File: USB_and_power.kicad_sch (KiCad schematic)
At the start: 44 parts, among them J1 USB_B_Micro, U1 LM2594M-3.3, U2 93LC54B, U3 FT4232H, Y1 12MHz

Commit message: After update to kicak 9.0
Signed-off-by: Marc Kelly <mpkelly@achenar.co.uk>
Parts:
- C1: MFN (none) -> Kemet; MFP (none) -> C0603C103J3RACAUTO; SUPPLIER (none) -> Mouser; SUPPLIER_LINK (none) -> https://www.mouser.co.uk/ProductDetail/KEMET/C0603C103J3RAC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; SUPPLIER_PN (none) -> 80-C0603C103J3RAUTO
- C10, C11, C12, C13, C14, C15, C16, C17, C18, C5, C7, C9: MFN (none) -> Kemet; MFP (none) -> C0603C104J4RACTU; SUPPLIER (none) -> Mouser; SUPPLIER_LINK (none) -> https://www.mouser.co.uk/ProductDetail/KEMET/C0603C104J4RAC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; SUPPLIER_PN (none) -> 80-C0603C104J4R
- C2: MFN (none) -> Kyocera AVX; MFP (none) -> TAJB686K010RNJ; Notes (none) -> 10V rated; SUPPLIER (none) -> Mouser; SUPPLIER_LINK (none) -> https://www.mouser.co.uk/ProductDetail/Kyocera-AVX/TAJB686K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; SUPPLIER_PN (none) -> 581-TAJB686K010RNJ
- C3: MFN (none) -> Panasonic; MFP (none) -> EEE-FN1A151L; Notes (none) -> 10V, 150uF; SUPPLIER (none) -> Mouser; SUPPLIER_LINK (none) -> https://www.mouser.co.uk/ProductDetail/Panasonic/EEE-FN1A15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; SUPPLIER_PN (none) -> 667-EEE-FN1A151L
- C4, C6: MFN (none) -> Kyocera AVX; MFP (none) -> F981C475MMA; SUPPLIER (none) -> Mouser; SUPPLIER_LINK (none) -> https://www.mouser.co.uk/ProductDetail/Kyocera-AVX/F981C475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; SUPPLIER_PN (none) -> 647-F981C475MMA
- C8: MFN (none) -> Kyocera AVX; MFP (none) -> TLCL335M016RTA; SUPPLIER (none) -> Mouser; SUPPLIER_LINK (none) -> https://www.mouser.co.uk/ProductDetail/Kyocera-AVX/TLCL335M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; SUPPLIER_PN (none) -> 581-TLCL335M016RTA
- D1: MFN (none) -> Samtech; MFP (none) -> RCLAMP0582BQTCT; SUPPLIER (none) -> Mouser; SUPPLIER_LINK (none) -> https://www.mouser.co.uk/ProductDetail/Semtech/RCLAMP0582BQ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; SUPPLIER_PN (none) -> 947-RCLAMP0582BQTCT
- D12, D2: MFN (none) -> Wurth; MFP (none) -> 155060GS75300; SUPPLIER (none) -> Mouser; SUPPLIER_LINK (none) -> https://www.mouser.co.uk/ProductDetail/Wurth-Elektronik/155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; SUPPLIER_PN (none) -> 710-155060GS75300
- D13: MFN (none) -> Wurth; MFP (none) -> 150060GS55040; SUPPLIER (none) -> Mouser; SUPPLIER_LINK (none) -> https://www.mouser.co.uk/ProductDetail/Wurth-Elektronik/150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; SUPPLIER_PN (none) -> 710-150060GS55040
- D3: MFN (none) -> MCC; MFP (none) -> MBRX120LF-TP; SUPPLIER (none) -> Mouser; SUPPLIER_LINK (none) -> https://www.mouser.co.uk/ProductDetail/Micro-Commercial-Com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; SUPPLIER_PN (none) -> 833-MBRX120LF-TP
- F1: MFN (none) -> Bel Fuse; MFP (none) -> 0ZCJ0075AF2E; SUPPLIER (none) -> Mouser; SUPPLIER_LINK (none) -> https://www.mouser.co.uk/ProductDetail/Bel-Fuse/0ZCJ0075AF2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; SUPPLIER_PN (none) -> 530-0ZCJ0075AF2E
- J1: MFN (none) -> Ampheonol; MFP (none) -> 10103594-0001LF; SUPPLIER (none) -> Mouser; SUPPLIER_LINK (none) -> https://www.mouser.co.uk/ProductDetail/Amphenol-FCI/1010359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; SUPPLIER_PN (none) -> 649-10103594-0001LF
- L1, L3, L4: MFN (none) -> TDK; MFP (none) -> MLZ1608DR47DTD25; Notes (none) -> 470-680nH Rage. 500-1000mA; SUPPLIER (none) -> Mouser; SUPPLIER_LINK (none) -> https://www.mouser.co.uk/ProductDetail/TDK/MLZ1608DR47DTD25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; SUPPLIER_PN (none) -> 810-MLZ1608DR47DTD25
- L2: MFN (none) -> Bourns; MFP (none) -> SRN6045-101M; SUPPLIER (none) -> Mouser; SUPPLIER_LINK (none) -> https://www.mouser.co.uk/ProductDetail/Bourns/SRN6045-101M?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; SUPPLIER_PN (none) -> 652-SRN6045-101M
- R1, R8: MFN (none) -> Generic; SUPPLIER (none) -> Mouser; SUPPLIER_LINK (none) -> https://www.mouser.co.uk/ProductDetail/Susumu/YJP-1608-R001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; SUPPLIER_PN (none) -> 754-YJP-1608-R001
- R2: MFN (none) -> Generic; SUPPLIER (none) -> Mouser; SUPPLIER_LINK (none) -> https://www.mouser.co.uk/ProductDetail/YAGEO/RT0603FRE0710R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; SUPPLIER_PN (none) -> 603-RT0603FRE0710RL
- R20, R29, R30: MFN (none) -> Generic; SUPPLIER (none) -> Mouser; SUPPLIER_PN (none) -> 754-RG1608P-331-BT5
- R3: value R10 -> 10R; MFN (none) -> Generic; SUPPLIER (none) -> Mouser; SUPPLIER_LINK (none) -> https://www.mouser.co.uk/ProductDetail/YAGEO/RT0603FRE0710R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; SUPPLIER_PN (none) -> 603-RT0603FRE0710RL
- R4, R5: MFN (none) -> Generic; SUPPLIER (none) -> Mouser; SUPPLIER_LINK (none) -> https://www.mouser.co.uk/ProductDetail/YAGEO/RT0402FRE1310K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; SUPPLIER_PN (none) -> 603-RT0402FRE1310KL
- R6: MFN (none) -> Generic; SUPPLIER (none) -> Mouser; SUPPLIER_LINK (none) -> https://www.mouser.co.uk/ProductDetail/TE-Connectivity-Hols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; SUPPLIER_PN (none) -> 279-CPF0603F2K0C1
- R7: MFN (none) -> Generic; SUPPLIER (none) -> Mouser; SUPPLIER_PN (none) -> 603-RT0603DRE0712KL
- U1: MFN (none) -> TI; MFP (none) -> LM2594M-3.3/NOPB; SUPPLIER (none) -> Mouser; SUPPLIER_LINK (none) -> https://www.mouser.co.uk/ProductDetail/Texas-Instruments/LM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; SUPPLIER_PN (none) -> 926-LM2594MX33NOPB
- U3: MFN (none) -> FTDIChip; MFP (none) -> FT4232HL; SUPPLIER (none) -> Mouser; SUPPLIER_LINK (none) -> https://www.mouser.co.uk/c/semiconductors/interface-ics/usb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; SUPPLIER_PN (none) -> 895-FT4232HL-TRAY
- Y1: MFN (none) -> Vishy; MFP (none) -> XT9MNLANA12M; SUPPLIER (none) -> Mouser; SUPPLIER_LINK (none) -> https://www.mouser.co.uk/ProductDetail/Vishay-Dale/XT9MNLAN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; SUPPLIER_PN (none) -> 73-XT49M1200-S
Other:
- note added: "Inductors L1,2,3 should be ~470-680nH. 500-1000mA"

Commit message: Updated to remove the level shifters
Just have 3v3 ttl outputs for now, trancievers will be on different
boards
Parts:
- removed J1: USB_B_Micro, Connector_USB:USB_Micro-B_Amphenol_10103594-0001LF_Horizontal, symbol Connector:USB_B_Micro
- added J5: USB_C_Receptacle_USB2.0_14P, symbol Connector:USB_C_Receptacle_USB2.0_14P
- added R21, R22: 5k1, Resistor_SMD:R_0603_1608Metric_Pad0.98x0.95mm_HandSolder, symbol Device:R_Small
- renumbered C12 to C1, C4 to C10, C5 to C11, C6 to C12, C7 to C13, C1 to C14, C10 to C15, C8 to C16, C9 to C17, C11 to C18, C13 to C2, C14 to C3, C15 to C4, C16 to C5, C17 to C6, C18 to C7, C2 to C8, C3 to C9, D3 to D13, D2 to D14, D1 to D15, D12 to D16, D13 to D17, L3 to L1, L4 to L2, L2 to L3, L1 to L4, R20 to R15, R2 to R16, R3 to R17, R4 to R18, R7 to R19, R1 to R20, R5 to R23, R6 to R24, R29 to R25, R30 to R26, R8 to R27, U1 to U3, U3 to U4, U2 to U5
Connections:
- net D+: now also D15.1 (K), R17.2, J5.A6 (D+), J5.B6 (D+); no longer D15.2 (K), R16.2
- net D-: now also D15.2 (K), R16.2, J5.A7 (D-), J5.B7 (D-); no longer D15.1 (K), R17.2
- net GND: now also J5.A1 (GND), J5.A12 (GND), J5.B1 (GND), J5.B12 (GND), R21.2, R22.2
- net at F1.2: now also J5.A4 (VBUS), J5.A9 (VBUS), J5.B4 (VBUS), J5.B9 (VBUS)
- net at R20.1: now also J5.S1 (SHIELD)
- new net: J5.A5 (CC1), R22.1
- new net: J5.B5 (CC2), R21.1
- no-connect marks 4 -> 3
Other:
- moved on the sheet: C10, C11, C12, C13, C14, C8, C9, D13, D14, D15, F1, L1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

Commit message: Updated power leds and external protection on Serial
Signed-off-by: Marc Kelly <mpkelly@achenar.co.uk>
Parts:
- removed D14: G_LED, LED_SMD:LED_0603_1608Metric_Pad1.05x0.95mm_HandSolder, symbol Device:LED
- removed R15: 330R, Resistor_SMD:R_0603_1608Metric_Pad0.98x0.95mm_HandSolder, symbol Device:R_Small
- added C17: 100nF, Capacitor_SMD:C_0603_1608Metric_Pad1.08x0.95mm_HandSolder, symbol Device:C_Small
- added SW1: ResetButton, Button_Switch_SMD:SW_SPST_TS-1088-xR020, symbol Switch:SW_Push
- C8: footprint Capacitor_Tantalum_SMD:CP_EIA-3528-21_Kemet-B_Pad1.50x2.35mm_HandSolder -> Capacitor_Tantalum_SMD:CP_EIA-3528-21_Kemet-B_HandSolder
- J5: footprint (none) -> Connector_USB:USB_C_Receptacle_HRO_TYPE-C-31-M-12; symbol Connector:USB_C_Receptacle_USB2.0_14P -> Connector:USB_C_Receptacle_USB2.0_16P
- Y1: value 12MHz -> ABLS7M2-12.000MHZ-D2Y-T; footprint Crystal:Crystal_SMD_HC49-SD_HandSoldering -> Crystal:Crystal_SMD_ECS_CSM3X-2Pin_7.6x4.1mm
- renumbered C17 to C18, C18 to C19, D13 to D19, D15 to D20, D16 to D21, D17 to D22, R16 to R17, R17 to R18, R18 to R19, R19 to R20, R20 to R21, R21 to R22, R22 to R23, R23 to R24, R24 to R25, R25 to R26, R26 to R27, R27 to R28
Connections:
- net D_N: now also R17.1; no longer R18.1
- net D_P: now also R18.1; no longer R17.1
- net GND: now also C17.2, SW1.1
- net RESET#: now also C17.1, SW1.2
- no-connect marks 3 -> 5
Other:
- note added: "Decoupling Caps"
- moved on the sheet: R19

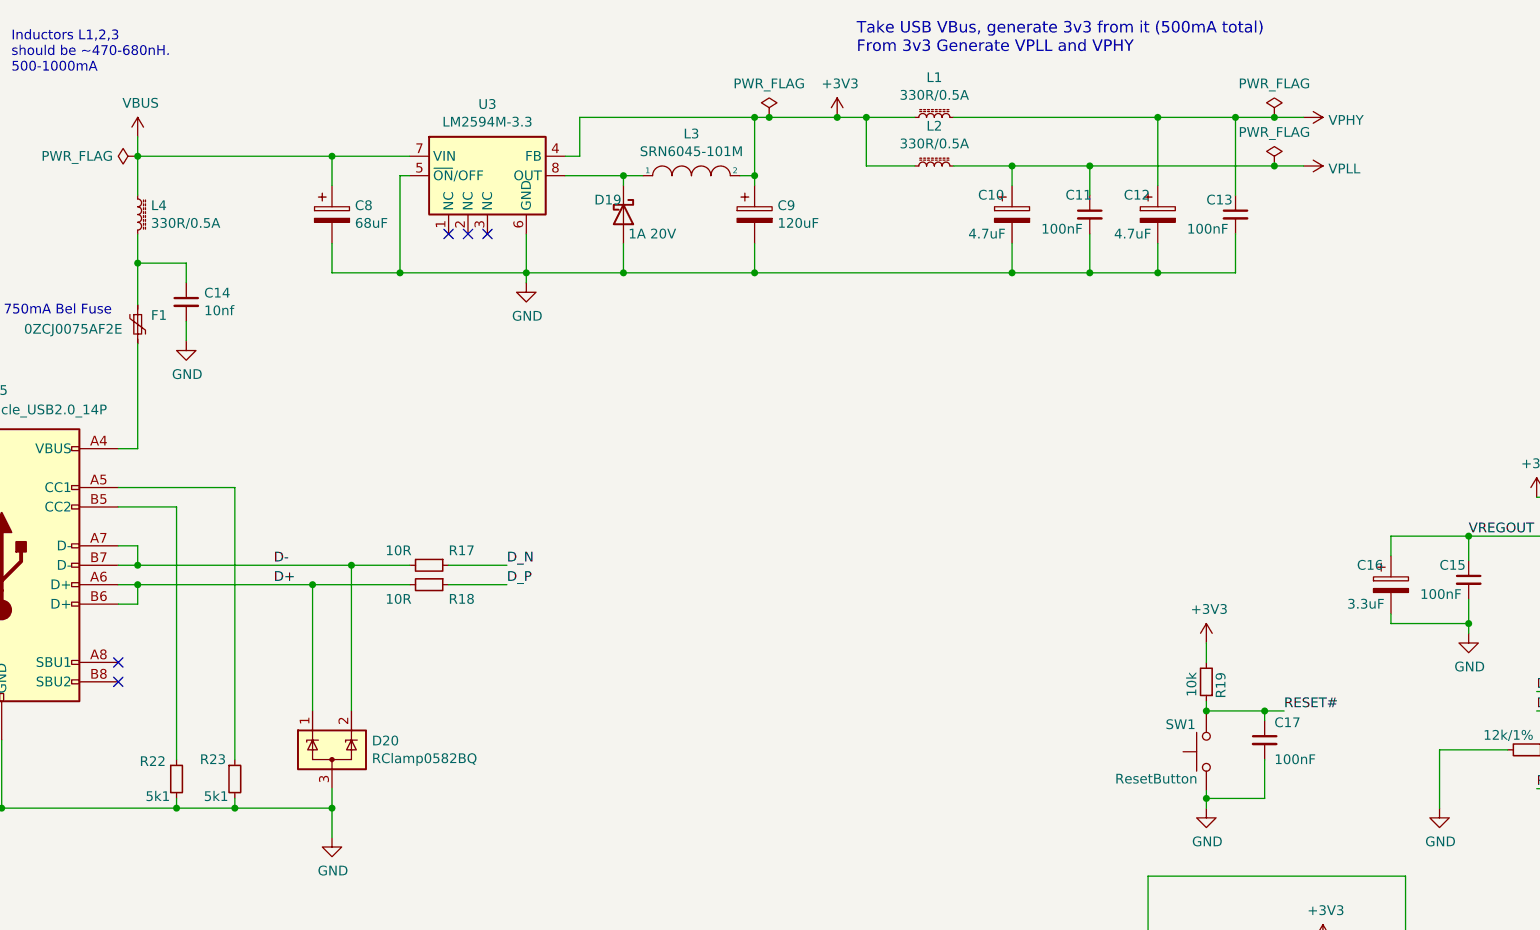
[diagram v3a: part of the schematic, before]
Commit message: Updated with the new design.
Removed all level translators.
4 sockets, 2x6 pin outputs
New PCB shape and routing
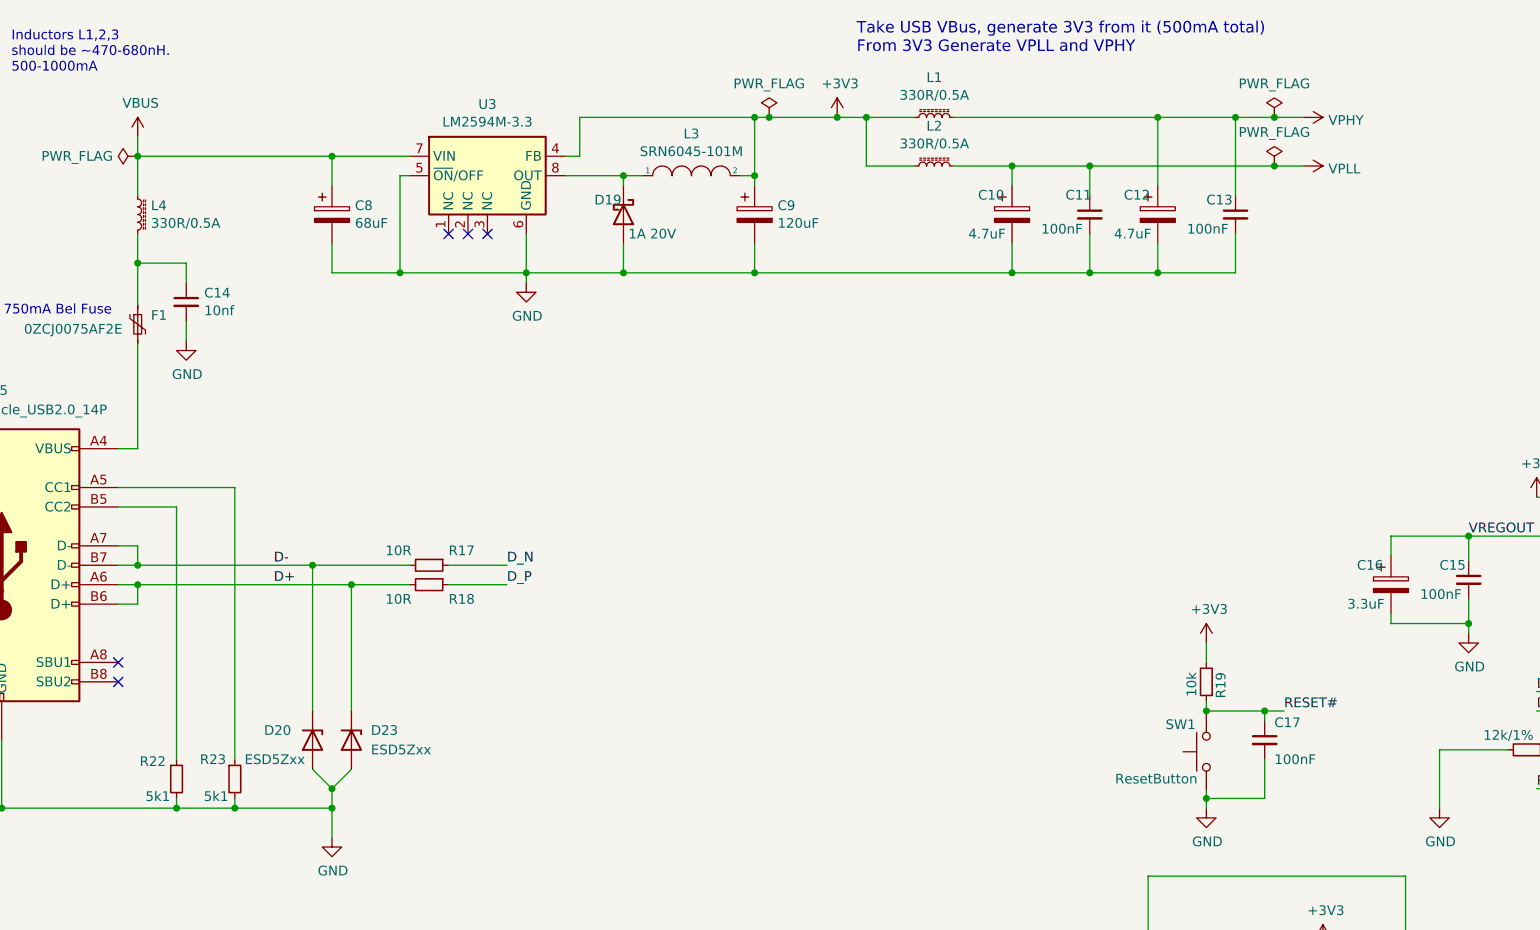
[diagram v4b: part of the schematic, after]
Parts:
- removed D20: RClamp0582BQ, Package_TO_SOT_SMD:SOT-416, symbol Power_Protection:SP0502BAJT
- added D20, D23: ESD5Zxx, Diode_SMD:D_SOD-523, symbol Diode:ESD5Zxx
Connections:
- net D+: now also D23.1 (K)
- net D-: now also D20.1 (K)
- net GND: now also D20.2 (A), D23.2 (A)
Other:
- note added: "Take USB VBus, generate 3V3 from it (500mA total) From 3V3 Generate VPLL and VPHY"
- note removed: "Take USB VBus, generate 3v3 from it (500mA total) From 3v3 Generate VPLL and VPHY"

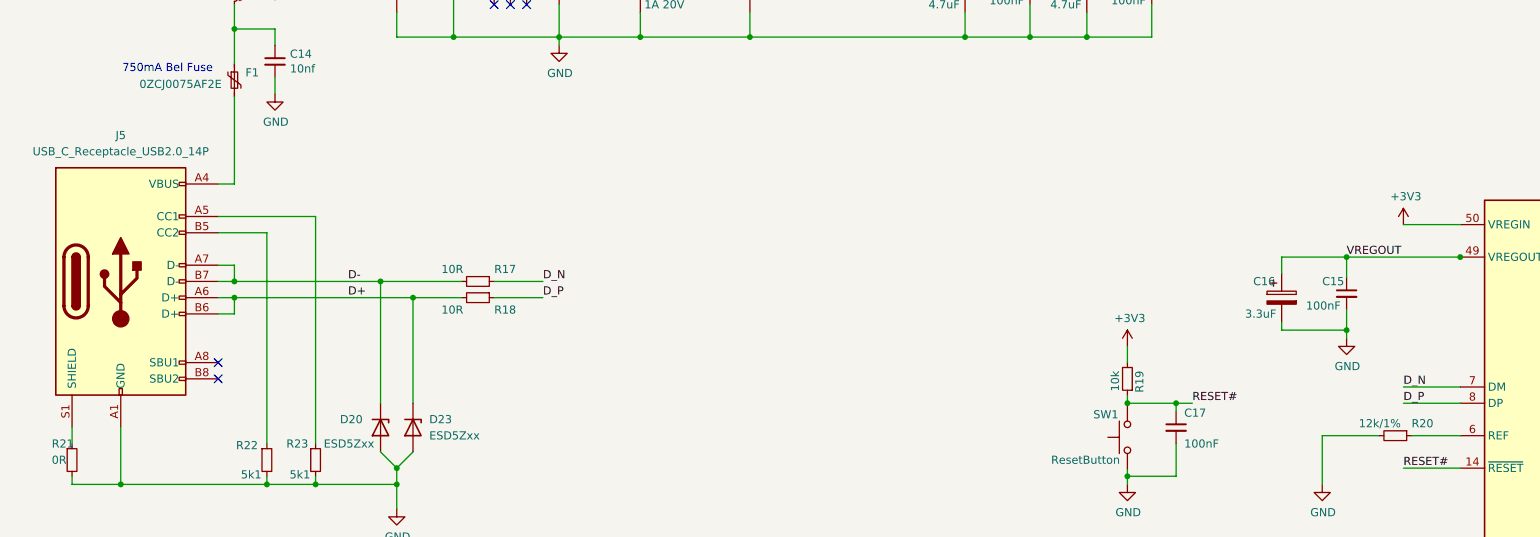
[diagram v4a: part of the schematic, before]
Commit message: Update schematics after moving to KiCad 10
Added some footprints to a local lib, as the silkscreen caused issues.

Signed-off-by: Marc Kelly <mpkelly@achenar.co.uk>
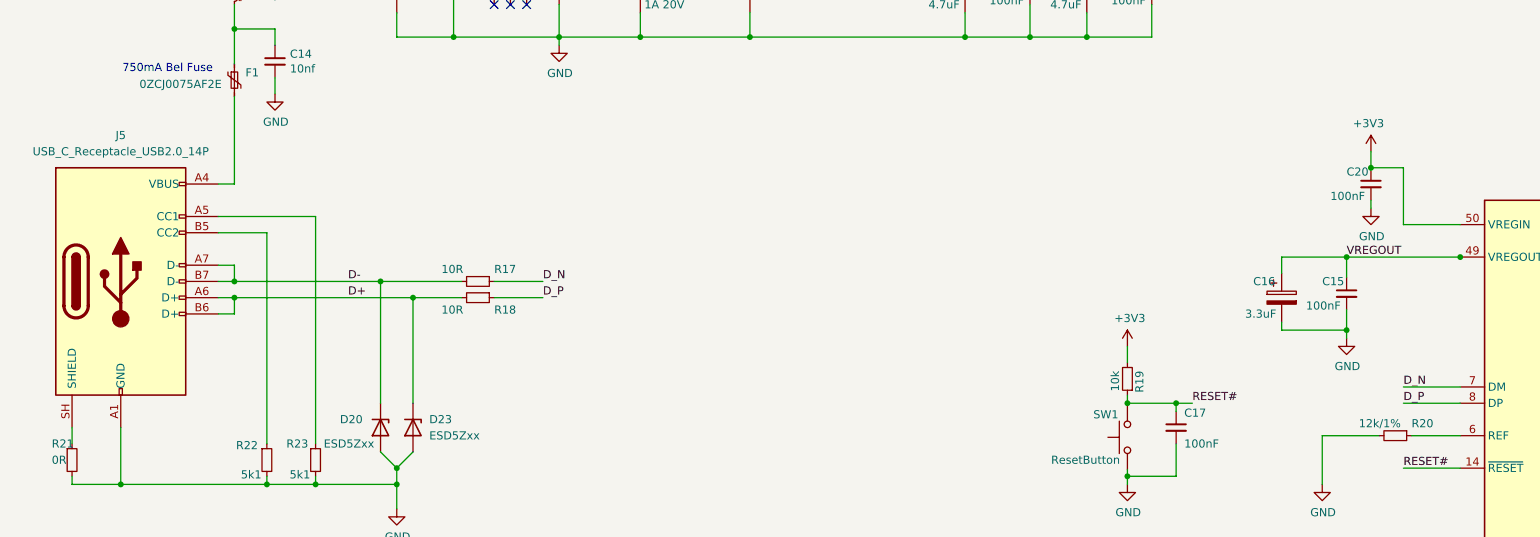
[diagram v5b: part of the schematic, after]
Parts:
- added C20: 100nF, Capacitor_SMD:C_0603_1608Metric_Pad1.08x0.95mm_HandSolder, symbol Device:C_Small
- J5: symbol Connector:USB_C_Receptacle_USB2.0_16P -> Connector:USB_C_Receptacle_USB2.0_14P
- L3: footprint Inductor_SMD:L_Bourns_SRN6045TA -> Local_FootPrints:L_Bourns_SRN6045TA
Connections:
- net +3V3: now also C20.1
- net GND: now also C20.2
- net at R21.1: now also J5.SH (SHIELD); no longer J5.S1 (SHIELD)
- no-connect marks 5 -> 3

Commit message: Sorting out BOMs
Signed-off-by: Marc Kelly <mpkelly@achenar.co.uk>
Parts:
- D20, D23: MFN (none) -> OnSemi; MFP (none) -> ESD5Z2.5T1G; SUPPLIER (none) -> Mouser; SUPPLIER_PN (none) -> 863-ESD5Z2.5T1G
- J5: MFN (none) -> Same Sky; MFP (none) -> UJ20-C-H-G-SMT-2A-P16-TR; SUPPLIER (none) -> Mouser; SUPPLIER_PN (none) -> 179-CHGSMT2AP16TR
- R17, R18: MFP (none) -> 10R 1%
- R19, R24: MFP (none) -> 10k 1%
- R20: MFP (none) -> 12k 1%
- R21, R28: MFP (none) -> 0R
- R22, R23: MFP (none) -> 5.1k 1%
- R25: MFP (none) -> 2k 1%
- SW1: MFN (none) -> GCT; MFP (none) -> SWT0110-020016SSA; SUPPLIER (none) -> Farnell; SUPPLIER_PN (none) -> 4715649
- U5: MFN (none) -> Microchip; MFP (none) -> 93LC56B-I/MS; SUPPLIER (none) -> Mouser; SUPPLIER_PN (none) -> 579-93LC56B-I/MS
